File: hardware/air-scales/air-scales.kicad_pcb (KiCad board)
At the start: 4 copper layers, 75 x 95 mm, 7 parts, among them J1 Connector, USB-TYPE-C-16P, U1 ESP32-S3-WROOM-2

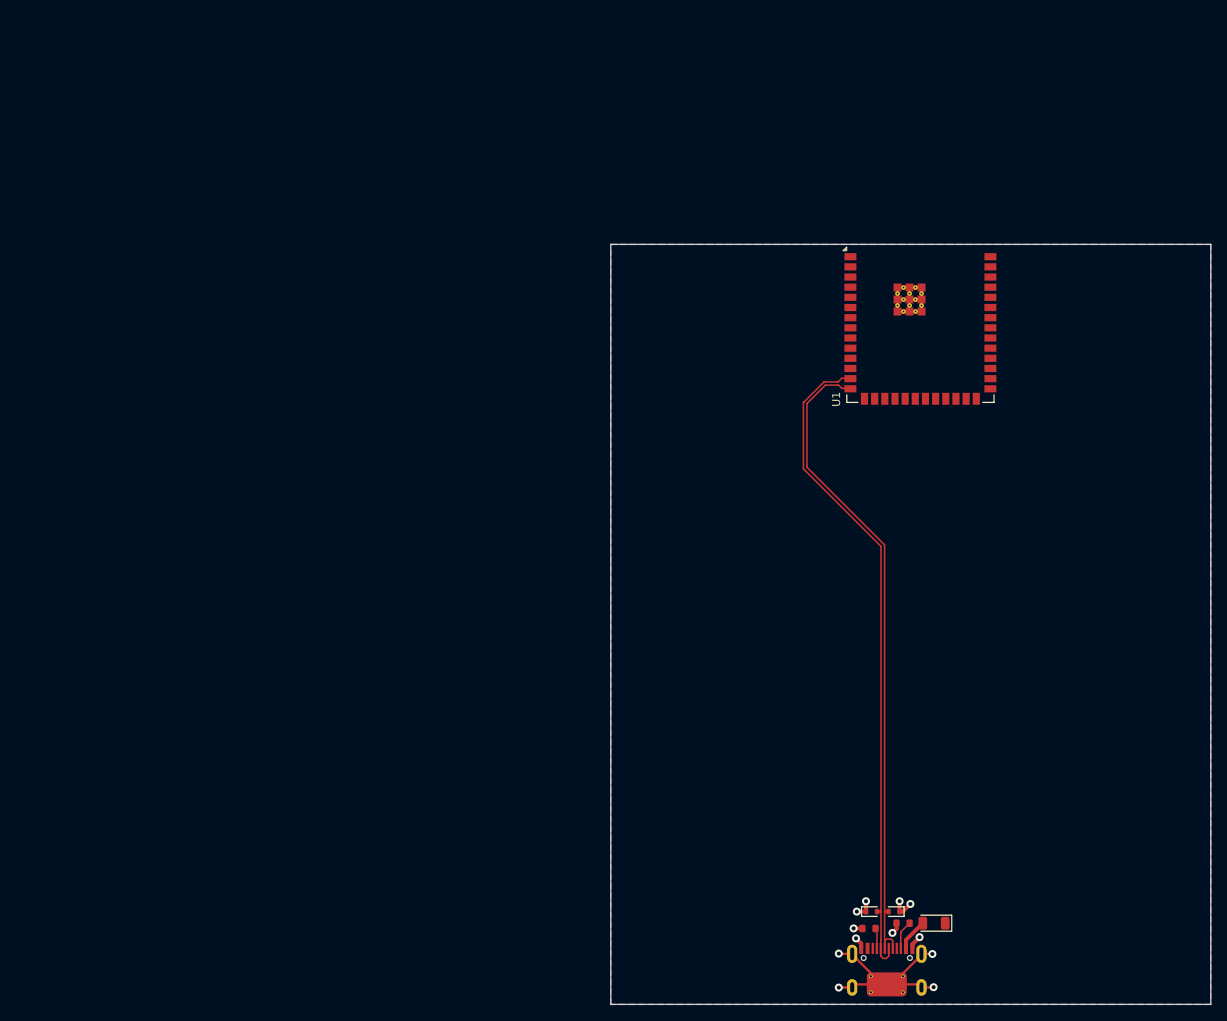
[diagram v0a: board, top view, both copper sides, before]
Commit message: pcb placement is done round 1
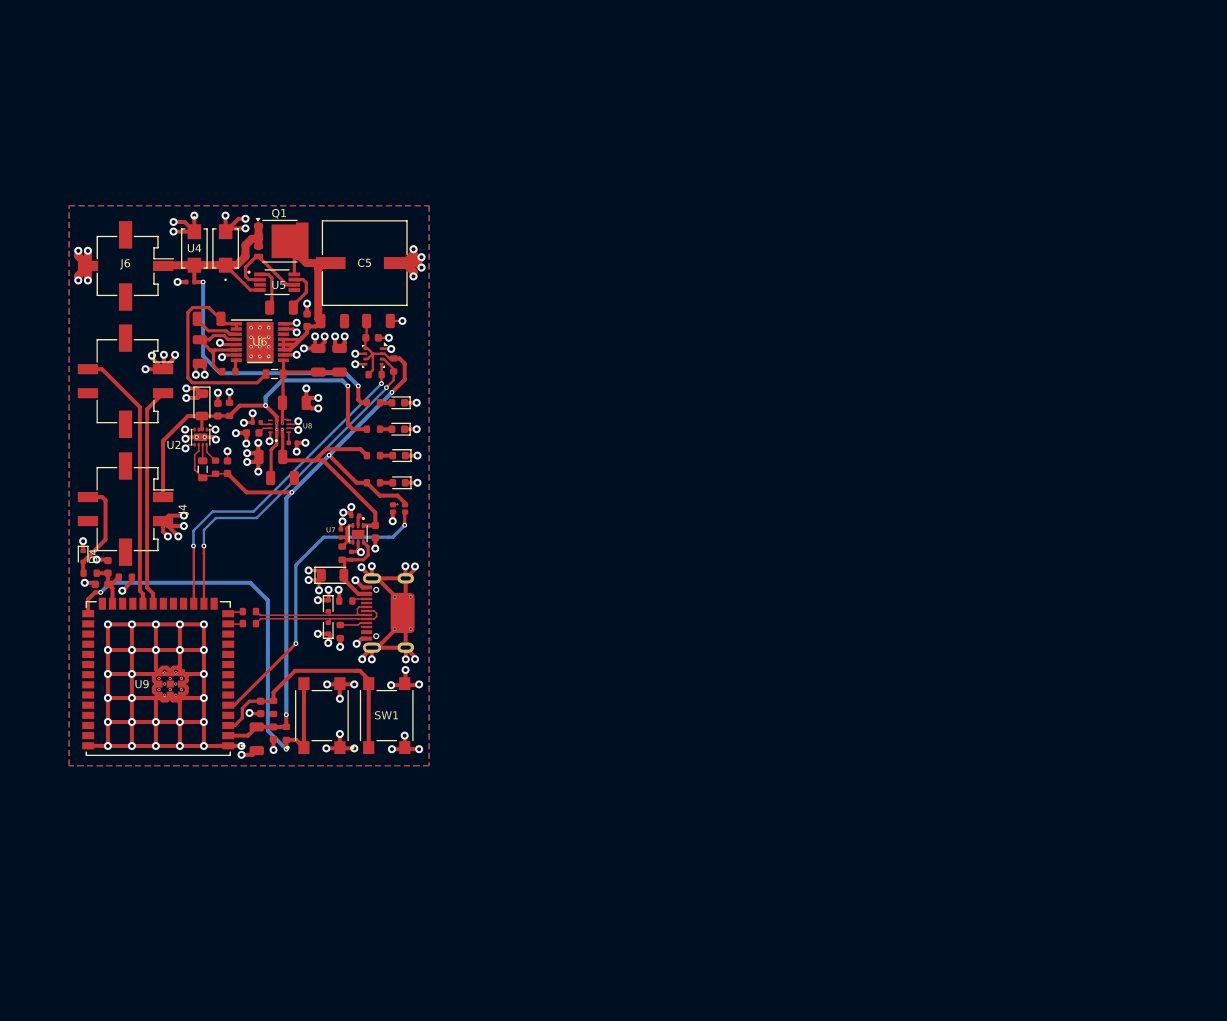
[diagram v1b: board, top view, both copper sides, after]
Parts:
- added C1: 10uF, PCM_JLCPCB:C_0603, F.Cu at (70.9, 85.7)
- added C10: 22uF, PCM_JLCPCB:C_1206, F.Cu at (83.4, 79.5)
- added C11: 22uF, PCM_JLCPCB:C_1206, F.Cu at (86.1, 79.5)
- added C12: 100nF, PCM_JLCPCB:C_0402, F.Cu at (87.6, 103.9)
- added C13: 120uF, PCM_JLCPCB:C_0603, F.Cu at (90.6, 100.9)
- added C14: 100nF, PCM_JLCPCB:C_0402, F.Cu at (86.3, 101.1)
- added C15: 100nF, PCM_JLCPCB:C_0402, F.Cu at (80.2, 89.8)
- added C16: 47nF, PCM_JLCPCB:C_0603, F.Cu at (75.2, 88.6)
- added C17: 22uF, PCM_JLCPCB:C_1206, F.Cu at (79.0, 94.2)
- added C18: 10uF, PCM_JLCPCB:C_1206, F.Cu at (75.7, 126.8)
- added C19: 100nF, PCM_JLCPCB:C_0603, F.Cu at (77.8, 126.1)
- added C2: 100pF, PCM_JLCPCB:C_0402, F.Cu at (67.4, 69.7)
- added C20: 1uF, PCM_JLCPCB:C_0603, F.Cu at (76.2, 122.9)
- added C21: 10nF, PCM_JLCPCB:C_0603, F.Cu at (56.3, 107.5)
- added C22: 100nF, PCM_JLCPCB:C_0603, F.Cu at (57.1, 105.3)
- added C23: 100nF, PCM_JLCPCB:C_0603, F.Cu at (90.2, 76.7)
- added C24: 10uF, PCM_JLCPCB:C_1206, F.Cu at (91.0, 74.6)
- added C25: 10uF, PCM_JLCPCB:C_1206, F.Cu at (80.4, 84.8)
- added C26: 10uF, PCM_JLCPCB:C_1206, F.Cu at (77.5, 91.6)
- added C3: 22uF, PCM_JLCPCB:C_0603, F.Cu at (72.1, 92.8)
- added C4: 2.2uF, PCM_JLCPCB:C_1206, F.Cu at (78.8, 72.9)
- added C5: 47uF, 10X12P7_NCH:CAP_PC_10X12P7_NCH, F.Cu at (89.2, 67.3)
- added C6: 10uF, PCM_JLCPCB:C_1206, F.Cu at (85.2, 74.6)
- added C7: 220nF, PCM_JLCPCB:C_0603, F.Cu at (82.0, 74.5)
- added C8: 1uF, PCM_JLCPCB:C_1206, F.Cu at (68.6, 78.4)
- added C9: 220nF, PCM_JLCPCB:C_1206, F.Cu at (69.8, 74.3)
- added D10: ESD441DPLR, PCM_JLCPCB:D_SOD-123FL, F.Cu at (68.9, 85.0)
- added D4: ESD5Z5.0, Diode_SMD:D_SOD-523, F.Cu at (54.0, 104.0)
- added D5: Red, PCM_JLCPCB:D_0603, F.Cu at (93.4, 84.8)
- added D6: GREEN, PCM_JLCPCB:D_0603, F.Cu at (93.4, 88.1)
- added D7: YELLOW, PCM_JLCPCB:D_0603, F.Cu at (93.5, 94.8)
- added D8: ORANGE, PCM_JLCPCB:D_0603, F.Cu at (93.5, 91.4)
- added D9: WS2812B, PCM_JLCPCB:LED-SMD_4P-L1.6-W1.5_XL-1615RGBC-WS2812B, F.Cu at (93.5, 98.0)
- added J3: Conn_02x02_Odd_Even, Connector_Molex:Molex_Micro-Fit_3.0_43045-0418_2x02-1MP_P3.00mm_Vertical, F.Cu at (59.3, 82.1)
- added J4: Conn_02x02_Odd_Even, Connector_Molex:Molex_Micro-Fit_3.0_43045-0418_2x02-1MP_P3.00mm_Vertical, F.Cu at (59.3, 98.1)
- added J6: Conn_02x01, Connector_Molex:Molex_Micro-Fit_3.0_43045-0218_2x01-1MP_P3.00mm_Vertical, F.Cu at (59.4, 67.7)
- added L1: 2.2uH,3.15A, PCM_JLCPCB:L_0805, F.Cu at (69.0, 93.1)
- added L2: 2.2uH,50mA, PCM_JLCPCB:L_0805, F.Cu at (78.0, 81.2)
- added Q1: C458246, Package_TO_SOT_SMD:LFPAK56, F.Cu at (78.6, 64.6)
- added R10: 100kΩ, PCM_JLCPCB:R_0603, F.Cu at (77.8, 122.9)
- added R11: 100kΩ, PCM_JLCPCB:R_0603, F.Cu at (79.4, 126.1)
- added R12: 27Ω, PCM_JLCPCB:R_0603, F.Cu at (74.8, 112.4)
- added R13: 27Ω, PCM_JLCPCB:R_0603, F.Cu at (74.8, 110.9)
- added R14: 4.7kΩ, PCM_JLCPCB:R_0603, F.Cu at (54.9, 106.1)
- added R15: 10kΩ, PCM_JLCPCB:R_0603, F.Cu at (59.3, 106.6)
- added R16: 10kΩ, PCM_JLCPCB:R_0603, F.Cu at (90.3, 84.8)
- added R17: 4.7kΩ, PCM_JLCPCB:R_0603, F.Cu at (92.9, 80.1)
- added R18: 4.7kΩ, PCM_JLCPCB:R_0603, F.Cu at (90.5, 81.3)
- added R19: 470Ω, PCM_JLCPCB:R_0603, F.Cu at (90.3, 94.8)
- added R20: 1kΩ, PCM_JLCPCB:R_0603, F.Cu at (90.3, 91.4)
- added R3: 1kΩ, PCM_JLCPCB:R_0603, F.Cu at (90.3, 88.1)
- added R4: 100kΩ, PCM_JLCPCB:R_0603, F.Cu at (72.3, 85.6)
- added R5: 100kΩ, PCM_JLCPCB:R_0603, F.Cu at (70.6, 92.8)
- added R6: 100kΩ, PCM_JLCPCB:R_0603, F.Cu at (72.3, 80.9)
- added R7: 100kΩ, PCM_JLCPCB:R_0603, F.Cu at (86.4, 103.6)
- added R8: 20kΩ, PCM_JLCPCB:R_0402, F.Cu at (88.1, 98.9)
- added R9: 20kΩ, PCM_JLCPCB:R_0402, F.Cu at (75.7, 87.3)
- added SW1: B3FS-1000, B3FS-1000:SW_B3FS-1000_OMR, F.Cu at (92.0, 123.9)
- added SW2: B3FS-1000, B3FS-1000:SW_B3FS-1000_OMR, F.Cu at (83.9, 123.9)
- added U2: TPS62162DSG, Package_SON:WSON-8-1EP_2x2mm_P0.5mm_EP0.9x1.6mm_ThermalVias, F.Cu at (68.7, 89.1)
- added U3: SMA6T28AY, SMA6T28AY:SMA_UNI_STM, F.Cu at (71.9, 65.5)
- added U4: SMA6T15AY, SMA6T28AY:SMA_UNI_STM, F.Cu at (68.0, 65.5)
- added U5: LM74610, LM74610QDGKTQ1:SOP65P490X110-8N, F.Cu at (78.3, 69.7)
- added U6: LM63625, LM63625:PWP0016K_N, F.Cu at (76.1, 77.2)
- added U7: TPS2553DRVR, TPS2553DRVR:SON65P200X200X80-7N, F.Cu at (88.4, 101.2)
- added U8: TPS2121RUXR, TPS2121RUXR:IC_TPS2121RUXR, F.Cu at (78.6, 87.7)
- added U9: ESP32-S3-WROOM-1U-N16R8, ESP32-S3-WROOM-1U-N16R8:XCVR_ESP32-S3-WROOM-1U-N16R8, F.Cu at (63.4, 119.3)
- J1: value Connector, USB-TYPE-C-16P -> USB-C
- U1: value ESP32-S3-WROOM-2 -> BME280; footprint RF_Module:ESP32-S3-WROOM-2 -> PCM_JLCPCB:Bosch_LGA-8_2.5x2.5mm_P0.65mm_ClockwisePinNumbering
- moved D3 86.8 mm to (85.2, 106.4), turned to 0 degrees
- moved R1 80.5 mm to (86.9, 109.6)
- moved D2 80.4 mm to (84.7, 110.2), turned to -90 degrees
- moved J1 76.7 mm to (92.0, 111.1), turned to 90 degrees
- moved D1 76.6 mm to (84.7, 113.0), turned to 90 degrees
- moved R2 75.8 mm to (86.2, 113.4), turned to -90 degrees
- moved U1 68.7 mm to (90.3, 79.0), turned to -90 degrees
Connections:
- net /CC1 renamed Net-(J1-CC1)
- net /CC2 renamed Net-(J1-CC2)
- net /USB_P renamed Net-(U7-IN)
- U1 pad 1: Net-(U1-GND-Pad1) -> GND
- U1 pad 2: unconnected-(U1-3V3-Pad2) -> +3.3V
- U1 pad 3: unconnected-(U1-EN-Pad3) -> /SDA
- U1 pad 4: unconnected-(U1-IO4-Pad4) -> /SCL
- U1 pad 5: unconnected-(U1-IO5-Pad5) -> GND
- U1 pad 6: unconnected-(U1-IO6-Pad6) -> +3.3V
- U1 pad 7: unconnected-(U1-IO7-Pad7) -> GND
- U1 pad 8: unconnected-(U1-IO15-Pad8) -> +3.3V
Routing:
- net GND: track 39.2 -> 398.6 mm, vias 12 -> 142
- net +3.3V: track 0.00 -> 102.4 mm, vias 0 -> 4
- net /D-: track 83.2 -> 17.7 mm
- net /D+: track 82.3 -> 17.6 mm
- net +12V BATT: track 0.00 -> 59.0 mm, vias 0 -> 2
- net /BOOT: track 0.00 -> 58.2 mm, vias 0 -> 2
- net +5V_SYS: track 0.00 -> 52.5 mm, vias 0 -> 2
- net /SDA: track 0.00 -> 44.3 mm, vias 0 -> 2
- net /SCL: track 0.00 -> 42.7 mm, vias 0 -> 2
- net /LED: track 0.00 -> 38.8 mm, vias 0 -> 2
- net /U0RXD: track 0.00 -> 33.2 mm
- net Net-(Q1-D): track 0.00 -> 32.9 mm
- net /EN: track 0.00 -> 31.0 mm
- net +5V USB: track 0.00 -> 27.8 mm
- net /U0TXD: track 0.00 -> 27.5 mm
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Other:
- board outline removed

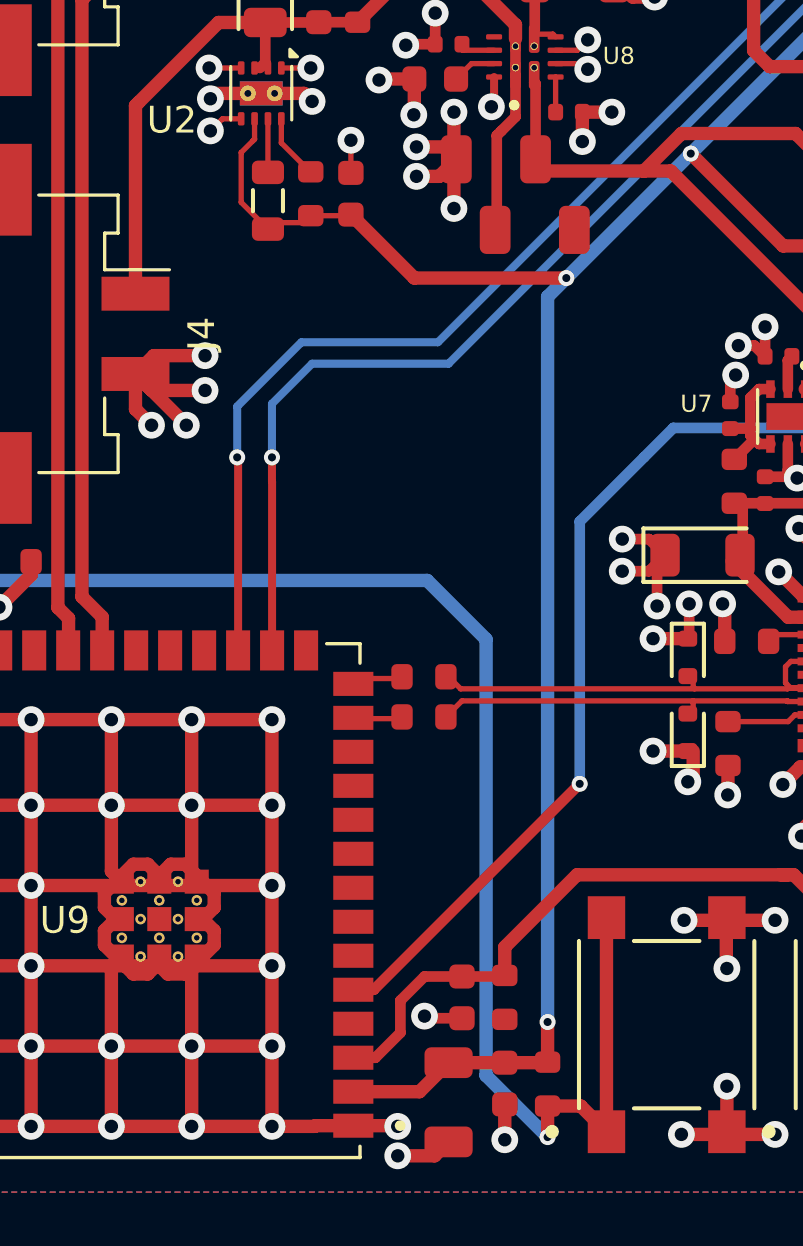
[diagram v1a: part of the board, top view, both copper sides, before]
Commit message: added pwr_flag to the power lines???
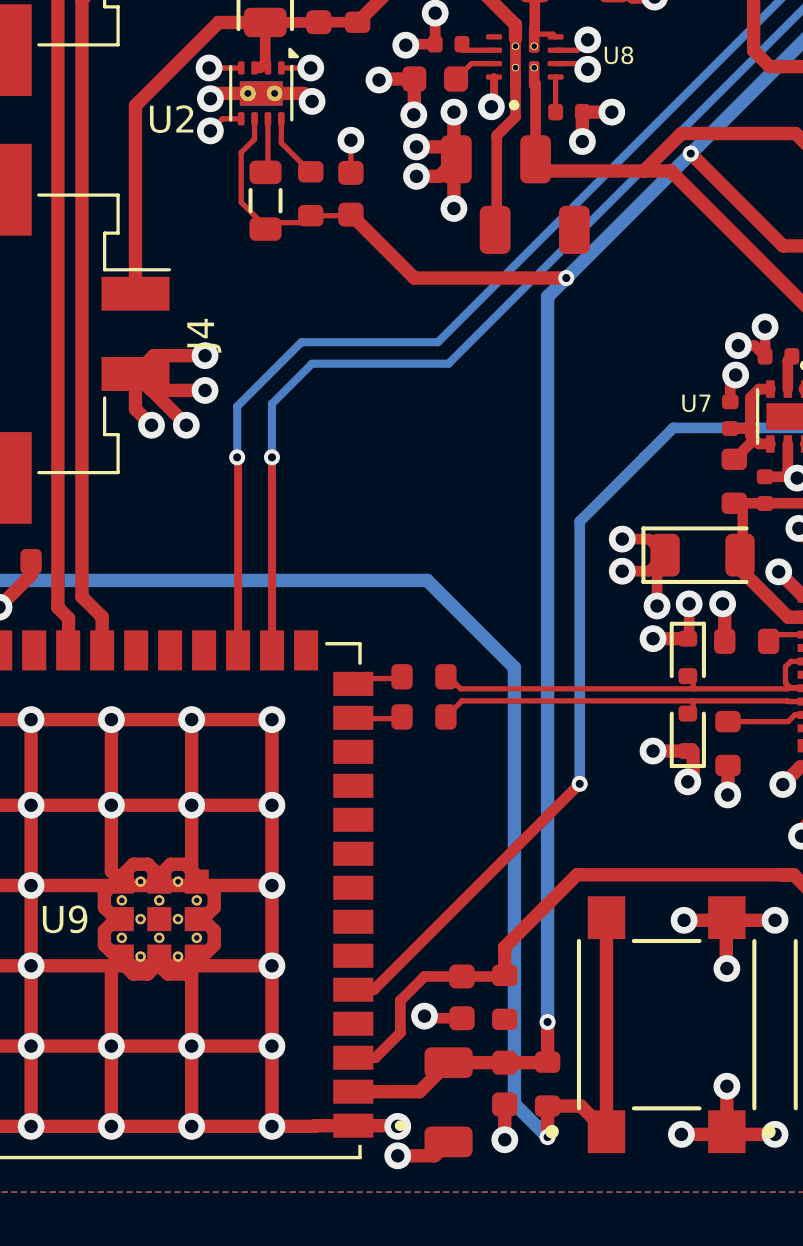
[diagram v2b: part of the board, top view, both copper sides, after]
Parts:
- moved L1 0.09 mm to (68.9, 93.1)
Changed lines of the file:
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@@
 	(footprint "PCM_JLCPCB:L_0805"
 		(layer "F.Cu")
-		(at 68.99 93.11 -90)
+		(at 68.9 93.11 -90)
 		(descr "Inductor SMD 0805 (2012 Metric), square (rectangular) end terminal, IPC_7351 nominal, (Body size source: IPC-SM-782 page 80, https://www.pcb-3d.com/wordpress/wp-content/uploads/ipc-sm-782a_amendment_1_and_2.pdf), generated with kicad-footprint-generator")
 		(tags "inductor")
@@
 	)
 	(segment
-		(start 77.14 109.5)
-		(end 77.14 125.8)
+		(start 78.2 126.86)
+		(end 79.44 128.1)
 		(width 0.5)
 		(layer "B.Cu")
@@
 	)
 	(segment
-		(start 57.44 107.3)
-		(end 74.94 107.3)
+		(start 56.24 108.5)
+		(end 57.44 107.3)
 		(width 0.5)
 		(layer "B.Cu")
@@
 	)
 	(segment
-		(start 56.24 108.5)
-		(end 57.44 107.3)
+		(start 57.44 107.3)
+		(end 74.94 107.3)
 		(width 0.5)
 		(layer "B.Cu")
@@
 	)
 	(segment
-		(start 77.14 125.8)
-		(end 79.44 128.1)
+		(start 74.94 107.3)
+		(end 78.2 110.56)
 		(width 0.5)
 		(layer "B.Cu")
@@
 	)
 	(segment
-		(start 74.94 107.3)
-		(end 77.14 109.5)
+		(start 78.2 110.56)
+		(end 78.2 126.86)
 		(width 0.5)
 		(layer "B.Cu")

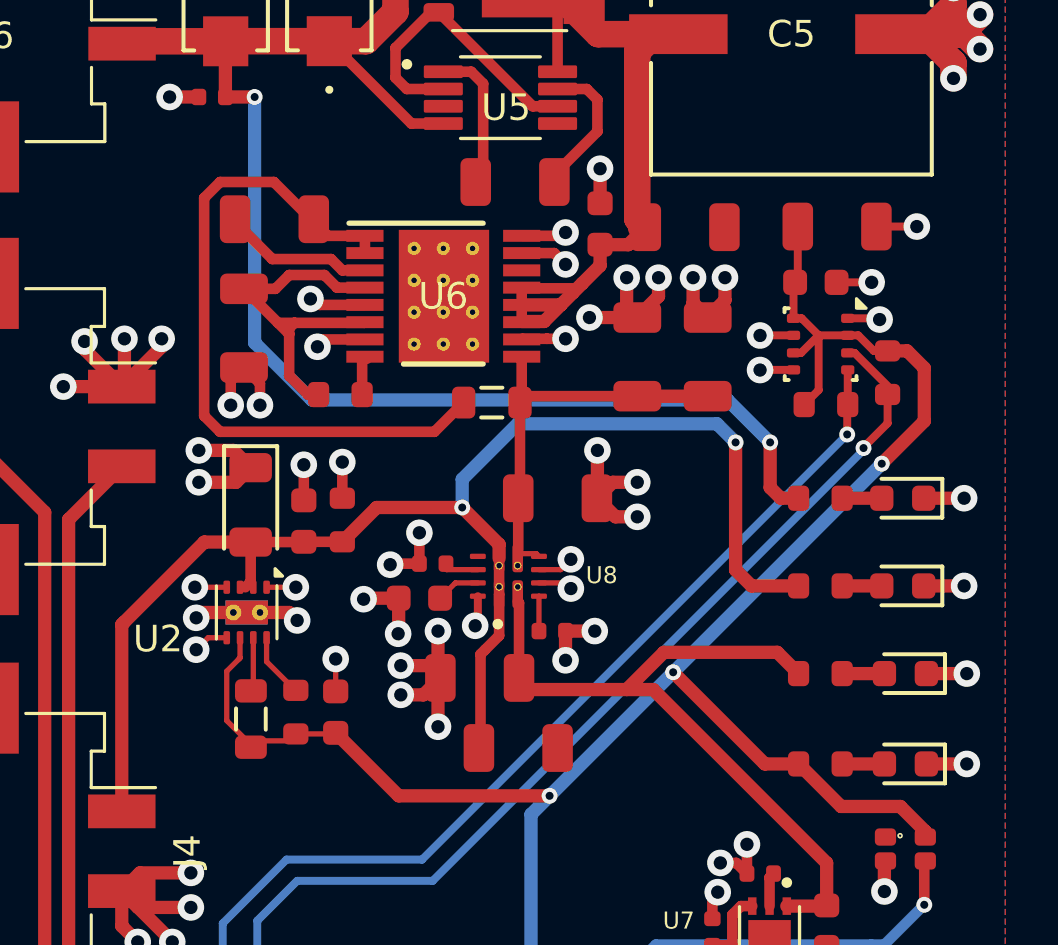
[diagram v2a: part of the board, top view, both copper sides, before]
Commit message: added pwr_flag to the power lines???
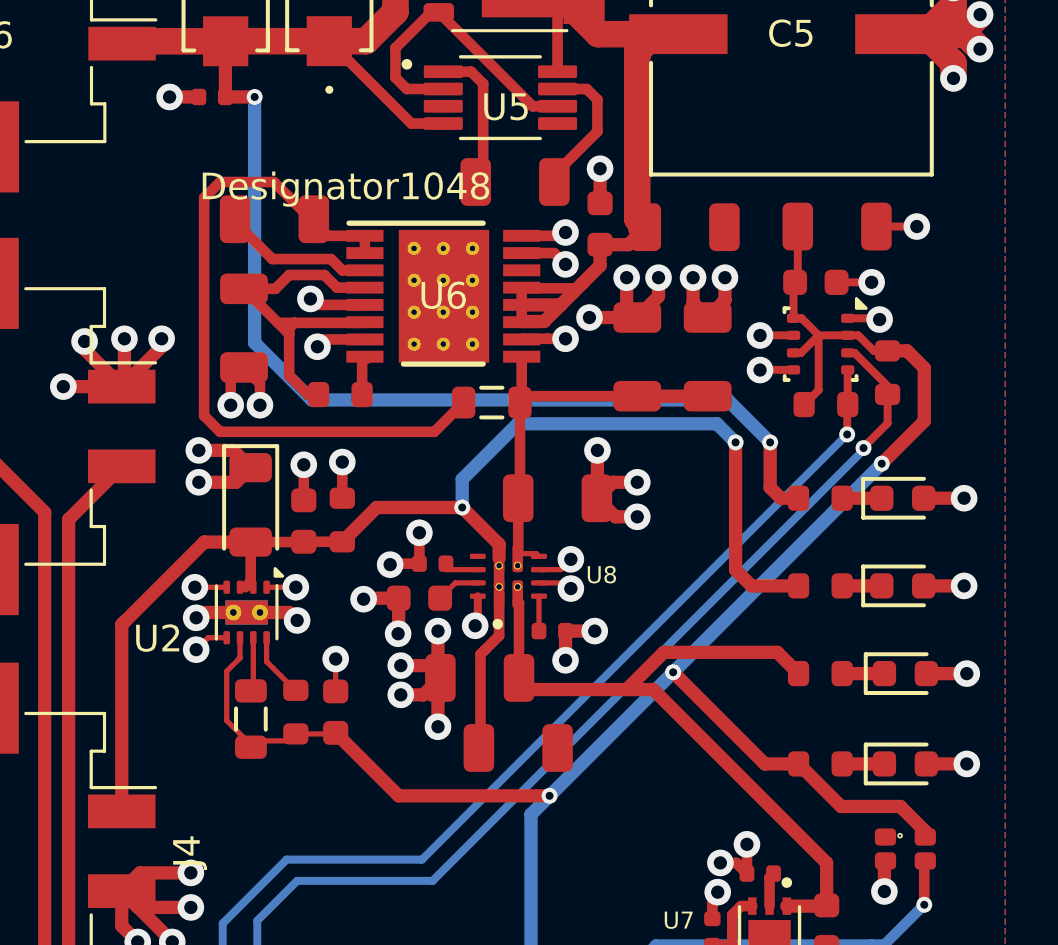
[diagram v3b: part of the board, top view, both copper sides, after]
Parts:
- J1: value USB-C -> Connector, USB-TYPE-C-16P
- U5: value LM74610 -> LM74610QDGKTQ1
- U6: value LM63625 -> LM63625DQPWPRQ1
- turned D5 to 0 degrees
- turned D6 to 0 degrees
- turned D7 to 0 degrees
- turned D8 to 0 degrees
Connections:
- C2 pad 2: GND -> Net-(U3-A)
- D5 pad 1: GND -> Net-(D5-Pad1)
- D5 pad 2: Net-(D5-Pad2) -> Net-(U3-A)
- D6 pad 1: GND -> Net-(D6-Pad1)
- D6 pad 2: Net-(D6-Pad2) -> GND
- D7 pad 1: GND -> Net-(D7-Pad1)
- D7 pad 2: Net-(D7-Pad2) -> GND
- D8 pad 1: GND -> Net-(D8-Pad1)
- D8 pad 2: Net-(D8-Pad2) -> GND
- R16 pad 2: Net-(D5-Pad2) -> Net-(D5-Pad1)
- R19 pad 2: Net-(D7-Pad2) -> Net-(D7-Pad1)
- R20 pad 2: Net-(D8-Pad2) -> Net-(D8-Pad1)
- R3 pad 2: Net-(D6-Pad2) -> Net-(D6-Pad1)
- U3 pad 2: GND -> Net-(U3-A)
- U4 pad 1: GND -> Net-(U3-A)
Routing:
- net Net-(U3-A): track 0.00 -> 18.2 mm, vias 0 -> 8
- net GND: track 398.6 -> 380.4 mm, vias 142 -> 134
- net Net-(D8-Pad2): track 1.59 -> 0.00 mm
- net Net-(D8-Pad1): track 0.00 -> 1.59 mm
- net Net-(D7-Pad2): track 1.59 -> 0.00 mm
- net Net-(D7-Pad1): track 0.00 -> 1.59 mm
- net Net-(D6-Pad2): track 1.49 -> 0.00 mm
- net Net-(D6-Pad1): track 0.00 -> 1.49 mm
- net Net-(D5-Pad2): track 1.49 -> 0.00 mm
- net Net-(D5-Pad1): track 0.00 -> 1.49 mm
